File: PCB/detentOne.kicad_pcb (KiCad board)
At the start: 4 copper layers, 150 x 85 mm, 88 parts, among them J1 Conn_01x07, J2 Conn_01x03, SW1 SW_Push, SW2 SW_Push, SW3 SW_Push, SW4 SW_Push, SW5 SW_Push, SW6 SW_Push, SW7 C92589, SW8 C92589, U2 SGM2050XTRL20G/TR, U3 ESP32-S3-WROOM-1(N16R8), U4 TMC6300-LA-T_C5274455, U5 XY-GH1.25-7A61, U6 PCA9554ARGVR, U7 AS5047P-ATSM_C962063

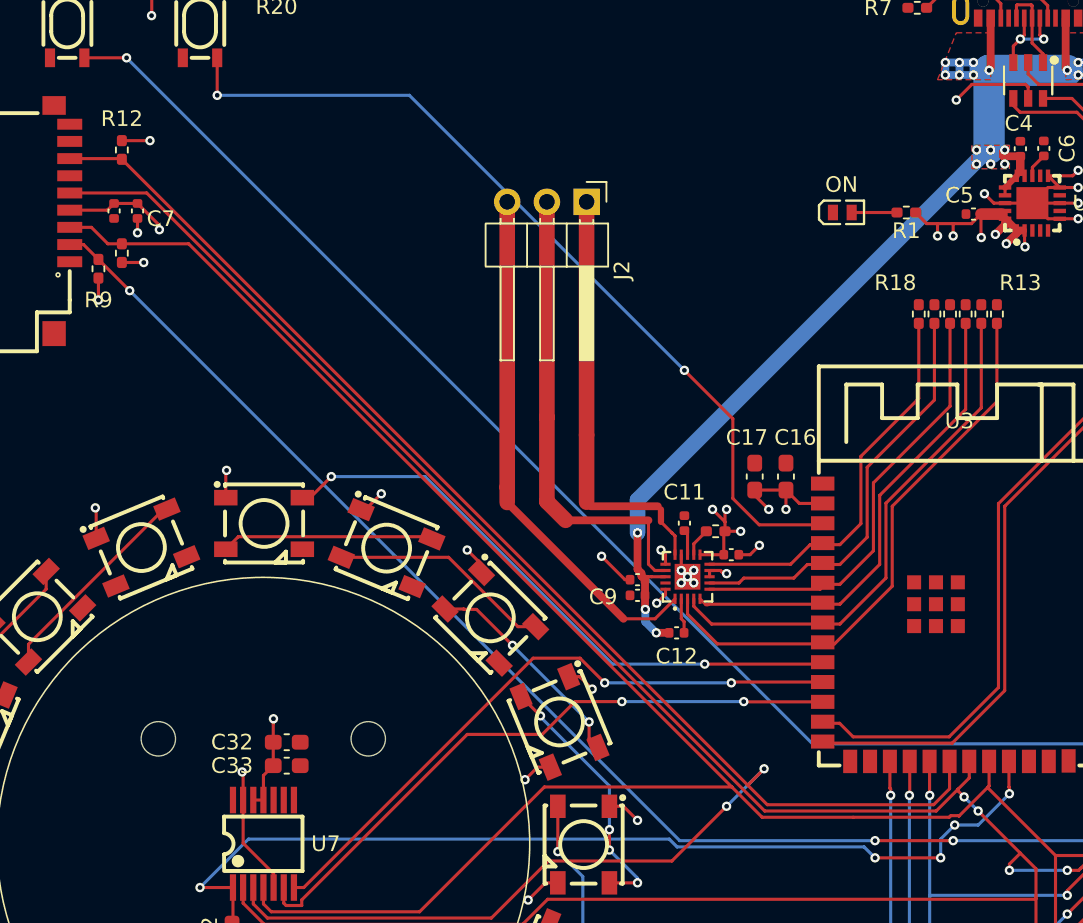
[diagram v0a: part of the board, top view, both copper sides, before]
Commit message: PCB traced - small changes still
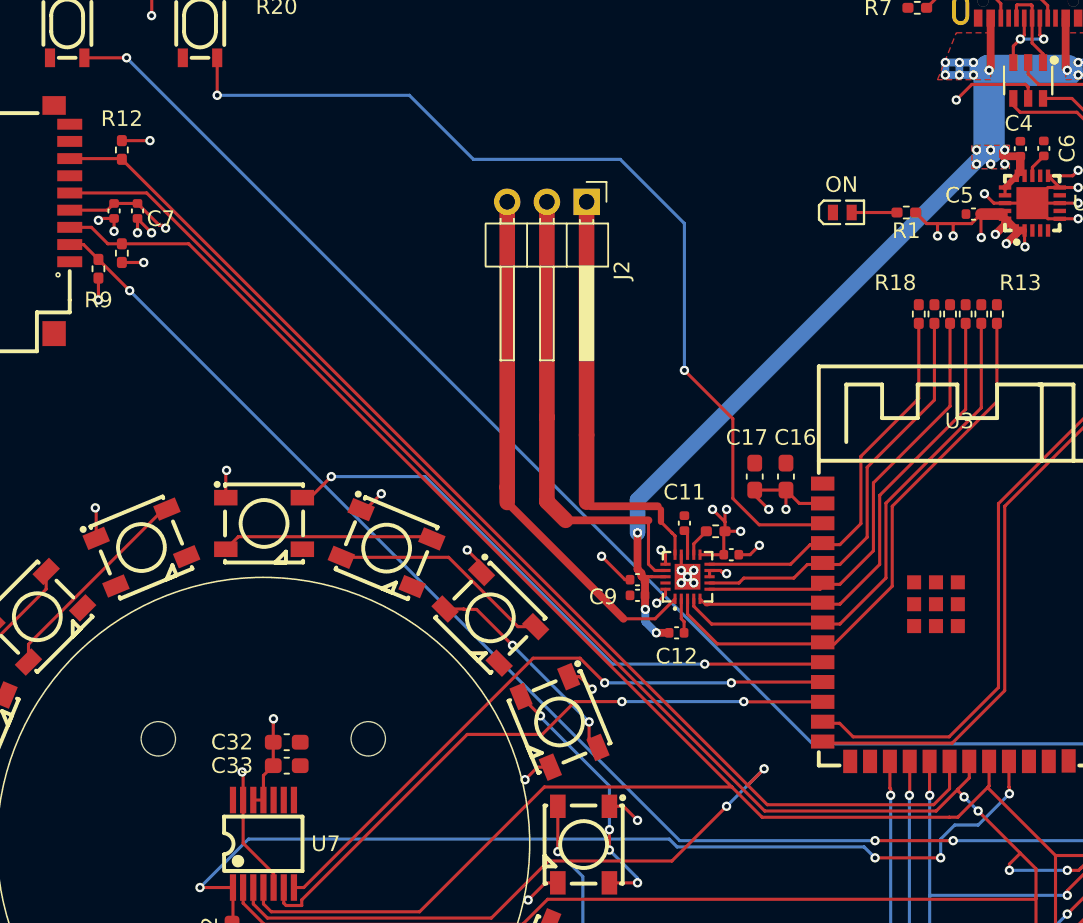
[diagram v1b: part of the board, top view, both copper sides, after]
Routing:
- net EN: track 61.1 -> 66.6 mm
- net GND: track 52.1 -> 55.3 mm, vias 21 -> 24
- net ENCODER_CS: vias 5 -> 4
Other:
- board text added: "Add test pads"
- board text added: "Add via stitching for GND"
- board text added: "Change to ESP32-WROOM-1U"
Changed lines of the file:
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@@
 		)
 	)
+	(gr_text "Add via stitching for GND"
+		(at 142.9 36.6 0)
+		(layer "User.1")
+		(effects
+			(font
+				(size 1 1)
+				(thickness 0.15)
+			)
+			(justify left bottom)
+		)
+	)
+	(gr_text "Change to ESP32-WROOM-1U"
+		(at 142.9 39.6 0)
+		(layer "User.1")
+		(effects
+			(font
+				(size 1 1)
+				(thickness 0.15)
+			)
+			(justify left bottom)
+		)
+	)
 	(gr_text "3V3 and GND, I2C pins go here"
 		(at 118.6 54 0)
@@
 		)
 	)
+	(gr_text "Add test pads\n"
+		(at 142.8 42.2 0)
+		(layer "User.1")
+		(effects
+			(font
+				(size 1 1)
+				(thickness 0.15)
+			)
+			(justify left bottom)
+		)
+	)
 	(gr_text "Width: 0.2mm\nSpacing: 0.1mm"
 		(at 162.2 64 0)
@@
 	)
 	(segment
+		(start 99.62 70.98)
+		(end 99.5 71.1)
+		(width 0.2)
+		(layer "F.Cu")
+		(net 2)
+	)
+	(segment
 		(start 156.8 70)
 		(end 156.2 69.4)
@@
 	)
 	(segment
+		(start 102 70.98)
+		(end 102 71)
+		(width 0.2)
+		(layer "F.Cu")
+		(net 2)
+	)
+	(segment
+		(start 100.5 70.98)
+		(end 100.5 71.8)
+		(width 0.2)
+		(layer "F.Cu")
+		(net 2)
+	)
+	(segment
 		(start 138.61 93.91)
 		(end 138.61 93.51)
@@
 	)
 	(segment
+		(start 102 71)
+		(end 102.9 71.9)
+		(width 0.2)
+		(layer "F.Cu")
+		(net 2)
+	)
+	(segment
 		(start 141.2 92.5)
 		(end 141.8 91.9)
@@
 	)
 	(segment
+		(start 100.5 70.98)
+		(end 99.62 70.98)
+		(width 0.2)
+		(layer "F.Cu")
+		(net 2)
+	)
+	(segment
 		(start 136.8 93.51)
 		(end 137.2 93.91)
@@
 	)
 	(via
+		(at 102.9 71.9)
+		(size 0.6)
+		(drill 0.3)
+		(layers "F.Cu" "B.Cu")
+		(net 2)
+	)
+	(via
 		(at 162.2 71)
 		(size 0.6)
@@
 	)
 	(via
+		(at 99.5 71.1)
+		(size 0.6)
+		(drill 0.3)
+		(layers "F.Cu" "B.Cu")
+		(net 2)
+	)
+	(via
 		(at 180.4 90.2)
 		(size 0.6)
@@
 	)
 	(via
+		(at 100.5 71.8)
+		(size 0.6)
+		(drill 0.3)
+		(layers "F.Cu" "B.Cu")
+		(net 2)
+	)
+	(via
 		(at 139.7 93.71)
 		(size 0.6)
@@
 	)
 	(segment
+		(start 103.62 71.42)
+		(end 103.4 71.42)
+		(width 0.2)
+		(layer "F.Cu")
+		(net 4)
+	)
+	(segment
 		(start 195.9 80.28)
 		(end 195.9 80.2)
@@
 	)
 	(segment
-		(start 139.5975 91)
-		(end 139.5975 90.3975)
+		(start 103.8 71.6)
+		(end 103.62 71.42)
 		(width 0.2)
 		(layer "F.Cu")
@@
 	)
 	(segment
-		(start 133.1 108.6)
-		(end 134 109.5)
+		(start 139.5975 91)
+		(end 139.5975 90.3975)
 		(width 0.2)
 		(layer "F.Cu")
@@
 	)
 	(segment
-		(start 102 70.02)
-		(end 103.4 71.42)
+		(start 133.1 108.6)
+		(end 134 109.5)
 		(width 0.2)
 		(layer "F.Cu")
@@
 	)
 	(segment
+		(start 103.4 71.42)
+		(end 102 70.02)
+		(width 0.2)
+		(layer "F.Cu")
+		(net 4)
+	)
+	(segment
 		(start 124.015359 93.640528)
 		(end 124.015359 93.115359)
@@
 	)
 	(segment
-		(start 103.4 71.42)
-		(end 103.4 71.7)
-		(width 0.2)
-		(layer "F.Cu")
-		(net 4)
-	)
-	(segment
 		(start 110.06 108.2)
 		(end 110.06 106.6275)
@@
 	)
 	(via
-		(at 103.4 71.7)
+		(at 103.8 71.6)
 		(size 0.6)
 		(drill 0.3)
@@
 	)
 	(segment
-		(start 119.4 63.1)
+		(start 132.9 67.2)
+		(end 137 71.3)
+		(width 0.2)
+		(layer "B.Cu")
+		(net 8)
+	)
+	(segment
+		(start 137 71.3)
 		(end 137 80.7)
 		(width 0.2)
@@
 	)
 	(segment
+		(start 123.5 67.2)
+		(end 132.9 67.2)
+		(width 0.2)
+		(layer "B.Cu")
+		(net 8)
+	)
+	(segment
+		(start 119.4 63.1)
+		(end 123.5 67.2)
+		(width 0.2)
+		(layer "B.Cu")
+		(net 8)
+	)
+	(segment
 		(start 97.6625 72.65)
 		(end 98.5475 72.65)
@@
 	)
 	(segment
-		(start 160.75 133.5)
-		(end 160.75 111.75)
+		(start 141.9738 109.303)
+		(end 153.947057 109.303)
 		(width 0.2)
 		(layer "F.Cu")
@@
 	)
 	(segment
-		(start 128.039 107.3646)
-		(end 140.0354 107.3646)
+		(start 160.75 133.5)
+		(end 160.75 111.75)
 		(width 0.2)
 		(layer "F.Cu")
@@
 	)
 	(segment
-		(start 141.9738 109.303)
-		(end 147.8 109.303)
+		(start 128.039 107.3646)
+		(end 140.0354 107.3646)
 		(width 0.2)
 		(layer "F.Cu")
@@
 	)
 	(segment
-		(start 153.947057 109.303)
-		(end 154.051057 109.199)
+		(start 140.0354 107.3646)
+		(end 141.9738 109.303)
+		(width 0.2)
+		(layer "F.Cu")
+		(net 12)
+	)
+	(segment
+		(start 154.5 109.3)
+		(end 156.4 107.4)
 		(width 0.2)
 		(layer "F.Cu")
@@
 	)
 	(segment
-		(start 154.574972 109.225028)
-		(end 156.4 107.4)
-		(width 0.2)
-		(layer "F.Cu")
-		(net 12)
-	)
-	(segment
-		(start 154.548943 109.199)
-		(end 154.574972 109.225028)
+		(start 100.1025 72.6025)
+		(end 101 72.6025)
 		(width 0.2)
 		(layer "F.Cu")
@@
 	)
 	(segment
-		(start 100.1025 72.6025)
-		(end 101 72.6025)
+		(start 153.950057 109.3)
+		(end 154.5 109.3)
 		(width 0.2)
 		(layer "F.Cu")
@@
 	)
 	(segment
-		(start 140.0354 107.3646)
-		(end 141.9738 109.303)
-		(width 0.2)
-		(layer "F.Cu")
-		(net 12)
-	)
-	(segment
-		(start 147.8 109.303)
-		(end 153.947057 109.303)
+		(start 153.947057 109.303)
+		(end 153.950057 109.3)
 		(width 0.2)
 		(layer "F.Cu")
@@
 	)
 	(segment
-		(start 154.051057 109.199)
-		(end 154.548943 109.199)
-		(width 0.2)
-		(layer "F.Cu")
-		(net 12)
-	)
-	(segment
 		(start 159.5 114.5)
 		(end 159.5 112.6)
@@
 		(size 0.6)
 		(drill 0.3)
-		(layers "F.Cu" "B.Cu")
-		(net 45)
-	)
-	(via
-		(at 154.3 109.8)
-		(size 0.6)
-		(drill 0.3)

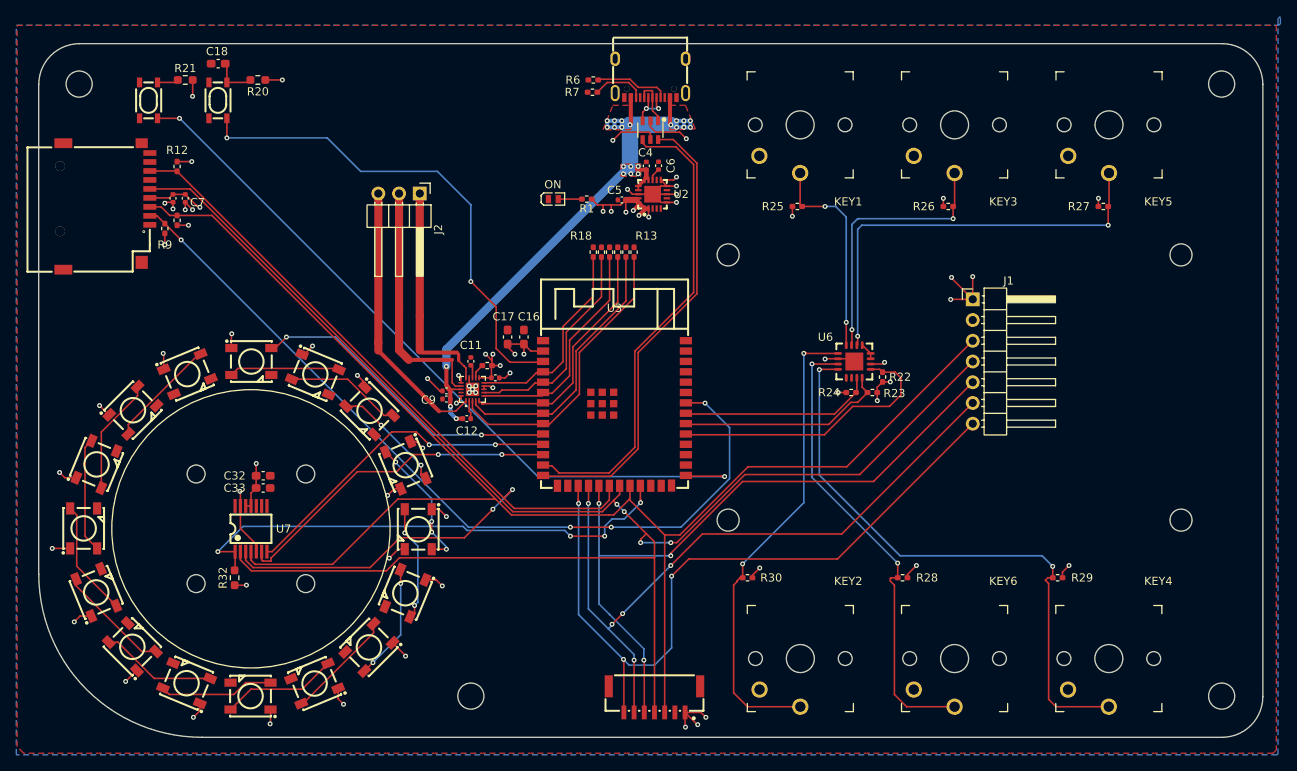
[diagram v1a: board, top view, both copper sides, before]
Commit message: silkscreen done
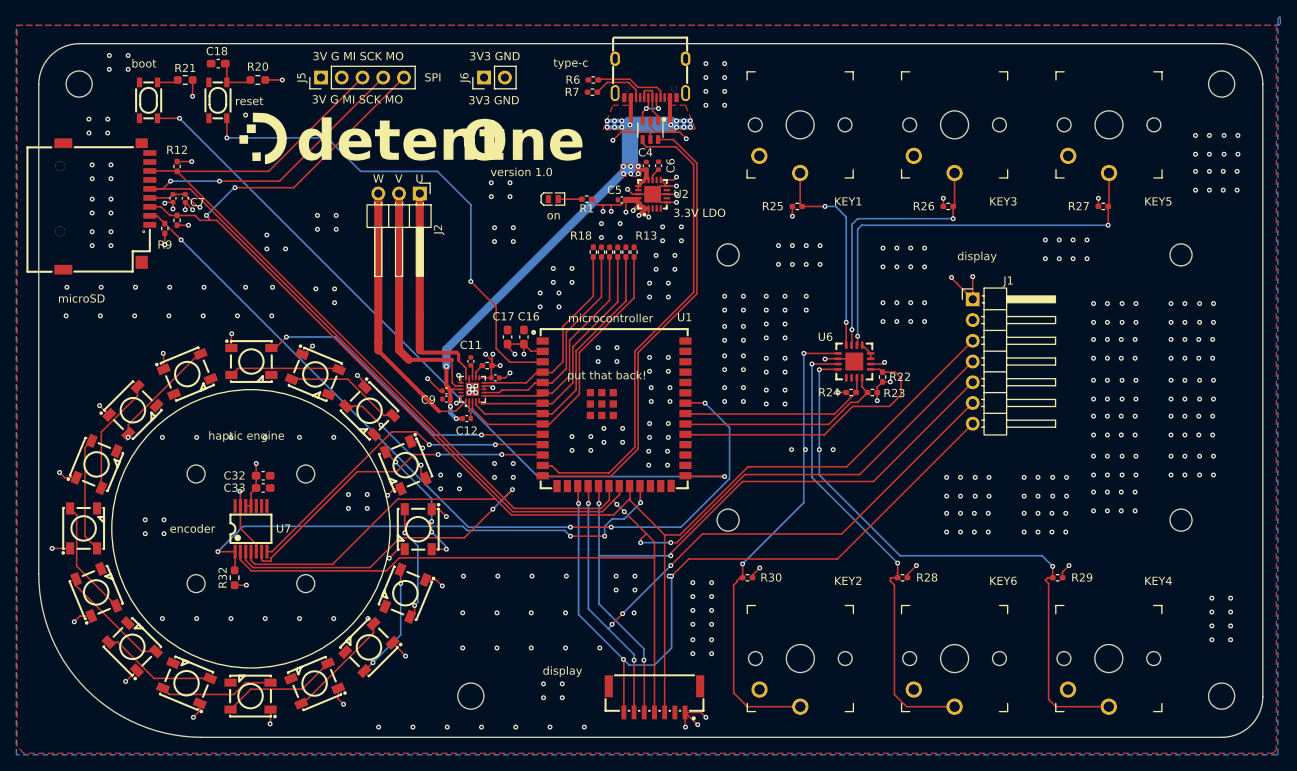
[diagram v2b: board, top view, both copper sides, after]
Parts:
- removed U3: ESP32-S3-WROOM-1(N16R8), easyeda2kicad:WIRELM-SMD_ESP32-S3-WROOM-1
- added J5: Conn_01x05, Connector_PinHeader_2.54mm:PinHeader_1x05_P2.54mm_Vertical, F.Cu at (118.6, 55.7)
- added J6: Conn_01x02, Connector_PinHeader_2.54mm:PinHeader_1x02_P2.54mm_Vertical, F.Cu at (138.6, 55.7)
- added U1: ESP32-S3-WROOM-1U-N16R8, easyeda2kicad:WIRELM-SMD_ESP32-S3-WROOM-1U, F.Cu at (154.6, 96.9)
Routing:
- net SCK: track 208.2 -> 242.5 mm, vias 4 -> 6
- net MOSI: track 186.9 -> 218.8 mm, vias 0 -> 2
- net MISO: track 115.2 -> 142.6 mm
- net 3V3: track 121.0 -> 118.3 mm, vias 52 -> 51
- net GND: vias 24 -> 423
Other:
- board text added: "3.3V LDO"
- board text added: "3V G MI SCK MO"
- board text added: "3V3 GND"
- board text added: "Add silkscreen text"
- board text added: "Made by humans on Earth"
- board text added: "One"
- board text added: "SPI"
- board text added: "U"
- board text added: "V"
- board text added: "W"
- board text added: "boot"
- board text added: "detent"
- board text added: "display"
- board text added: "encoder"
- board text added: "haptic engine"
- board text added: "microSD"
- board text added: "microcontroller"
- board text added: "on"
- board text added: "put that back!"
- board text added: "reset"
- board text added: "type-c"
- board text added: "version 1.0"
- board text added: "version 1.0 9th feb 2026"
- board text added: "{ "ViaStitching": "0.2", "stitch_zone_0": { "HSpacing": "4", "VSpacing": "4", "HOffset": "0", "VOffset": "0", "Clearance": "0.25", "Randomize": false } }"
- board text added: "{ "ViaStitching": "0.2", "stitch_zone_0": { "HSpacing": "5", "VSpacing": "5", "HOffset": "0", "VOffset": "0", "Clearance": "0", "Randomize": false } }"
- board text added: "{dblquote}Stay hungry, stay foolish.{dblquote}"
- board text removed: "3V3 and GND, I2C pins go here"
- board text removed: "Add test pads"
- board text removed: "Add via stitching for GND"
- board text removed: "Change to ESP32-WROOM-1U"
- board text removed: "Don't run traces under Antenna!"
- board text removed: "ON"
- board text removed: "Replace with WROOM-1U Variant"

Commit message: Update detentOne.kicad_pcb
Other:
- board text removed: "Add silkscreen text"
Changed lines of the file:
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@@
-		)
-	)
-	(gr_text "Add silkscreen text"
-		(at 142.7 43.3 0)
-		(layer "User.1")
-		(effects
-			(font
-				(size 1 1)
-				(thickness 0.15)
-			)
-			(justify left bottom)
 		)
 	)

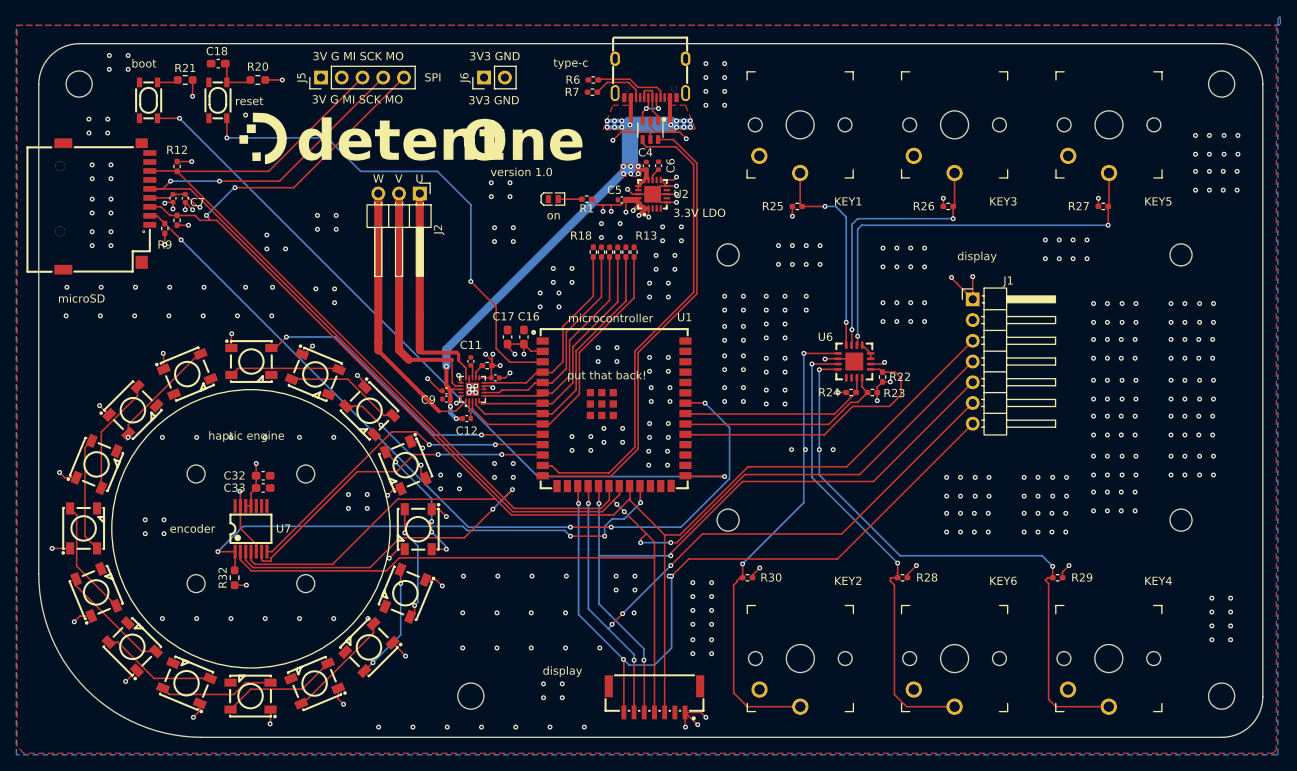
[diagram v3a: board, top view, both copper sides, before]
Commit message: added bulk caps + drc check
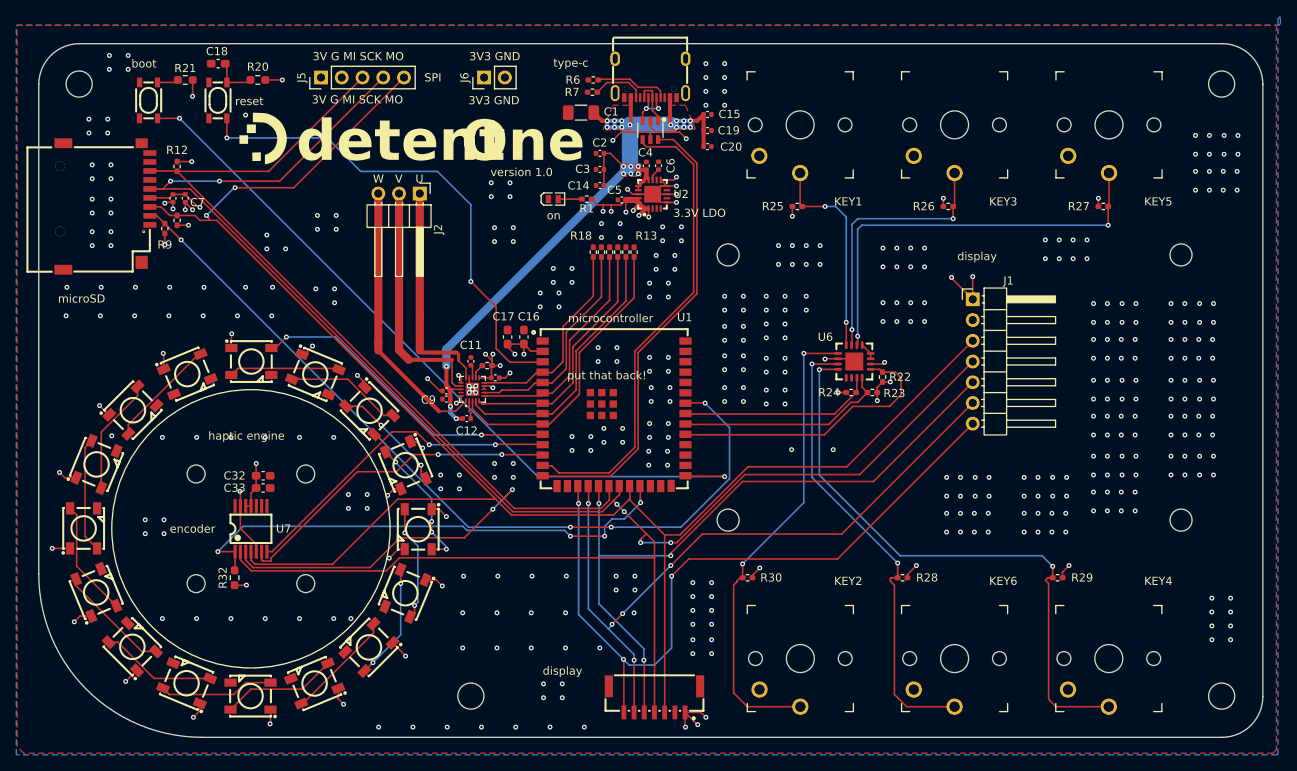
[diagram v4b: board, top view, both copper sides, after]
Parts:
- added C1: 100uF 6.3V, Capacitor_SMD:C_1206_3216Metric_Pad1.33x1.80mm_HandSolder, F.Cu at (150.5, 60.0)
- added C14: 10uF 10V, Capacitor_SMD:C_0402_1005Metric, F.Cu at (152.8, 68.9)
- added C15: 10uF 10V, Capacitor_SMD:C_0402_1005Metric, F.Cu at (166.0, 60.2)
- added C19: 10uF 10V, Capacitor_SMD:C_0402_1005Metric, F.Cu at (166.0, 62.2)
- added C2: 10uF 10V, Capacitor_SMD:C_0402_1005Metric, F.Cu at (152.8, 65.0)
- added C20: 10uF 10V, Capacitor_SMD:C_0402_1005Metric, F.Cu at (166.0, 64.2)
- added C3: 10uF 10V, Capacitor_SMD:C_0402_1005Metric, F.Cu at (152.8, 67.0)
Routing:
- net 5V: track 80.0 -> 94.9 mm
- net GND: vias 423 -> 420
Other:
- board text added: "Add bulk capacitance to 5V in"

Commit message: Updated back silkscreen
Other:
- board text added: "*Made by humans on Earth*"
- board text removed: "Made by humans on Earth"
